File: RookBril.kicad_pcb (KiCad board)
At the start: 2 copper layers, 63 parts, among them J1 BATT_PINS, J10 UNCONNECTED_PB_PINS, J11 UNCONNECTED_PC_PINS, J12 PROGRAM_PINS, J13 3V_MODE_PINS, J2 IR_SENSOR0_PINS, J3 IR_SENSOR1_PINS, J4 IR_SENSOR2_PINS, J5 IR_SENSOR3_PINS, J6 LOW-BAT_LED_CONN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

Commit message: beginsel aan pcb gemaakt
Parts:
- added C24: 100n, Capacitor_SMD:C_0805_2012Metric_Pad1.18x1.45mm_HandSolder, F.Cu at (111.9, 149.8)
- J12: value PROGRAM_PINS -> Conn_01x04_Pin; footprint Connector_PinHeader_2.54mm:PinHeader_2x05_P2.54mm_Vertical -> Connector_PinHeader_2.54mm:PinHeader_1x04_P2.54mm_Vertical
- moved J1 120.0 mm to (30.7, 156.8), turned to 180 degrees
- moved J4 116.5 mm to (187.8, 156.0)
- moved R5 114.5 mm to (184.0, 155.8)
- moved R4 113.6 mm to (37.2, 160.5), turned to -90 degrees
- moved R3 112.0 mm to (37.0, 155.3), turned to -90 degrees
- moved C3 109.0 mm to (40.7, 160.5), turned to -90 degrees
- moved R1 108.3 mm to (184.0, 135.2)
- moved J12 107.3 mm to (135.9, 155.6)
- moved J2 107.0 mm to (187.8, 135.2)
- moved C13 105.5 mm to (106.7, 166.2), turned to 180 degrees
- moved J5 105.5 mm to (187.8, 145.7)
- moved R6 105.3 mm to (184.0, 145.5)
- moved C4 104.0 mm to (179.8, 156.8), turned to -90 degrees
- moved R2 99.8 mm to (184.0, 125.2)
- moved C15 97.0 mm to (99.9, 165.5), turned to 180 degrees
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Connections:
- J12 pad 1: +3V0 -> /MCU/SWDIO
- J12 pad 2: GND -> /MCU/SDCLK
- J12 pad 3: GND -> /MCU/NRST
- J12 pad 4: unconnected-(J12-Pin_4-Pad4) -> GND
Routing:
- net +3V0: track 0.00 -> 106.8 mm, vias 0 -> 6
- net /MCU/NRST: track 0.00 -> 55.0 mm
- net /MCU/SDCLK: track 0.00 -> 38.2 mm
- net +BATT: track 0.00 -> 29.8 mm
- net /MCU/SWDIO: track 0.00 -> 28.0 mm
- net VCC: track 0.00 -> 27.3 mm
- net VDDA: track 0.00 -> 18.5 mm
- net GND: track 0.00 -> 16.2 mm, vias 0 -> 2
- net Net-(D1-A): track 0.00 -> 15.1 mm
- net /PDLC-BOOST_VOUT-FB: track 0.00 -> 11.3 mm
- net /PDLC-BOOST_CTRL: track 0.00 -> 9.11 mm
- net /VBAT_FB: track 0.00 -> 6.87 mm
- net Net-(U2-FB): track 0.00 -> 5.89 mm
- net Net-(U4-FB): track 0.00 -> 5.52 mm
- net Net-(U4-MODE): track 0.00 -> 5.35 mm
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- added copper zone on B.Cu, net GND
- added copper zone on F.Cu, net GND

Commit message: Alle verbindingen gelegt van de componenten.
Moet nog bij nog tekst bij de connectoren zetten. Ook zijn de unconnected pinnen weggehaald, omdat het onmogelijk maakt voor een 2 laags PCB.
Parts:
- removed C19: 4.7u, Capacitor_SMD:C_0805_2012Metric_Pad1.18x1.45mm_HandSolder
- removed J11: UNCONNECTED_PC_PINS, Connector_PinHeader_1.00mm:PinHeader_1x14_P1.00mm_Vertical
- removed J8: UNCONNECTED_PA_PINS, Connector_PinHeader_1.00mm:PinHeader_1x07_P1.00mm_Vertical
- J10: value UNCONNECTED_PB_PINS -> TIM3_OUT_CONN; footprint Connector_PinHeader_1.00mm:PinHeader_1x13_P1.00mm_Vertical -> Connector_PinHeader_2.54mm:PinHeader_1x04_P2.54mm_Vertical
- moved C10 132.3 mm to (169.5, 86.3), turned to 180 degrees
- moved R11 130.4 mm to (169.5, 88.6), turned to 0 degrees
- moved R9 130.1 mm to (165.9, 87.2)
- moved C7 130.0 mm to (163.5, 82.9), turned to -90 degrees
- moved R12 129.2 mm to (162.5, 86.0)
- moved U2 128.5 mm to (166.1, 83.1)
- moved L1 127.5 mm to (166.7, 77.5)
- moved D1 126.9 mm to (171.4, 80.5)
- moved C8 126.5 mm to (169.5, 84.1)
- moved C6 112.4 mm to (162.5, 90.6), turned to 180 degrees
- moved R10 112.0 mm to (158.8, 89.6)
- moved R8 111.5 mm to (162.5, 88.3), turned to 0 degrees
- moved C9 110.7 mm to (158.4, 86.0), turned to 0 degrees
- moved R14 110.1 mm to (130.3, 91.3), turned to 90 degrees
- moved J7 109.0 mm to (176.7, 99.3)
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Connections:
- J10 pad 1: /MCU/PB2 -> /MCU/PB0
- J10 pad 2: /MCU/PB3 -> /MCU/PB1
- U3 pad 26: /IR_SIG2 -> /MCU/PB0
- U3 pad 27: /IR_SIG3 -> /MCU/PB1
- U3 pad 28: /MCU/PB2 -> /IR_SIG2
- U3 pad 30: Net-(U3-VCAP1) -> unconnected-(U3-VCAP1-Pad30)
- U3 pad 55: /MCU/PB3 -> /IR_SIG3
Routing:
- net +3V0: track 106.8 -> 170.6 mm, vias 6 -> 7
- net +BATT: track 29.8 -> 88.5 mm, vias 0 -> 1
- net /PDLC-BOOST_CTRL: track 9.11 -> 53.2 mm, vias 0 -> 2
- net /MCU/PB1: track 0.00 -> 38.5 mm, vias 0 -> 1
- net /MCU/PB0: track 0.00 -> 35.3 mm, vias 0 -> 1
- net /MCU/PB4: track 0.00 -> 35.0 mm, vias 0 -> 1
- net /MCU/PB5: track 0.00 -> 34.2 mm, vias 0 -> 1
- net /IR_SIG2: track 0.00 -> 32.7 mm, vias 0 -> 2
- net GND: track 16.2 -> 48.4 mm, vias 2 -> 32
- net /H-BRIDGE_IN_A: track 0.00 -> 32.1 mm, vias 0 -> 4
- net /IR_SIG3: track 0.00 -> 30.4 mm
- net /IR_SIG1: track 0.00 -> 28.3 mm
- net /VBAT_FB: track 6.87 -> 34.7 mm, vias 0 -> 2
- net /H-BRIDGE_SEL: track 0.00 -> 25.2 mm, vias 0 -> 2
- net Net-(J9-Pin_2): track 0.00 -> 24.9 mm
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- added copper zone on F.Cu, net +BATT
- added copper zone on F.Cu, net /PDLC-BOOST_VOUT-FB
- added copper zone on F.Cu, net VCC
- added copper zone on F.Cu, net VDDA
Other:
- board outline added: 65 x 55 mm

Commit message: nieuwe layout
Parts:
- moved J3 52.0 mm to (119.8, 95.9), turned to 180 degrees
- moved J6 47.8 mm to (118.5, 117.8)
- moved J9 47.5 mm to (105.6, 63.3)
- moved J12 46.9 mm to (129.6, 115.4), turned to 90 degrees
- moved R2 46.2 mm to (124.1, 96.0), turned to 180 degrees
- moved C2 45.0 mm to (124.0, 93.7)
- moved R17 43.8 mm to (134.7, 47.5)
- moved R14 43.8 mm to (132.5, 47.6)
- moved R16 43.8 mm to (137.8, 46.7)
- moved C22 43.8 mm to (136.0, 43.1)
- moved C23 43.8 mm to (130.6, 43.2)
- moved R15 43.8 mm to (129.2, 46.8)
- moved L2 43.8 mm to (133.2, 40.6)
- moved U4 43.8 mm to (133.3, 43.3)
- moved J2 39.1 mm to (119.8, 104.9), turned to 180 degrees
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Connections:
- U3 pad 15: /H-BRIDGE_IN_A -> /H-BRIDGE_IN_B
- U3 pad 16: /H-BRIDGE_IN_B -> /H-BRIDGE_IN_A
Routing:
- net +3V0: track 170.6 -> 27.6 mm, vias 7 -> 0
- net +BATT: track 88.5 -> 0.00 mm, vias 1 -> 0
- net /MCU/PB1: track 38.5 -> 0.00 mm, vias 1 -> 0
- net /MCU/PB0: track 35.3 -> 0.00 mm, vias 1 -> 0
- net /MCU/PB4: track 35.0 -> 0.00 mm, vias 1 -> 0
- net /VBAT_FB: track 34.7 -> 0.00 mm, vias 2 -> 0
- net /MCU/PB5: track 34.2 -> 0.00 mm, vias 1 -> 0
- net /IR_SIG2: track 32.7 -> 0.00 mm, vias 2 -> 0
- net /PDLC-BOOST_CTRL: track 53.2 -> 20.8 mm
- net /IR_SIG1: track 28.3 -> 0.00 mm
- net Net-(J9-Pin_2): track 24.9 -> 0.00 mm
- net /MCU/NRST: track 45.6 -> 21.6 mm, vias 2 -> 0
- net /IR_SIG3: track 30.4 -> 10.5 mm
- net /MCU/SDCLK: track 30.4 -> 13.6 mm, vias 2 -> 0
- net /IR_SIG0: track 16.7 -> 0.00 mm
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- removed copper zone on F.Cu, net /PDLC-BOOST_VOUT-FB
- removed copper zone on F.Cu, net VDDA
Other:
- board text added: "NRST"
- board text added: "RESET"
- board text added: "SDCLK"
- board text added: "SWD"
- board text added: "SWDIO"

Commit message: betere
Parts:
- moved J9 72.0 mm to (148.4, 121.2), turned to -90 degrees
- moved J10 64.2 mm to (168.7, 96.9), turned to 0 degrees
- moved R3 44.2 mm to (132.2, 89.2)
- moved R4 44.2 mm to (132.2, 93.4)
- moved C3 44.2 mm to (136.0, 93.4)
- moved J13 39.6 mm to (130.5, 71.3), turned to 90 degrees
- moved R15 38.2 mm to (134.1, 84.6)
- moved J1 36.6 mm to (124.7, 81.4)
- moved C22 36.5 mm to (135.4, 79.6)
- moved C23 36.5 mm to (130.0, 79.7)
- moved R16 36.5 mm to (137.2, 83.2)
- moved L2 36.5 mm to (132.6, 77.1)
- moved R17 36.5 mm to (134.1, 84.0)
- moved U4 36.5 mm to (132.6, 79.8)
- moved R14 36.5 mm to (131.9, 84.1)
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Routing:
- net GND: track 34.7 -> 26.4 mm, vias 23 -> 24
- net VCC: track 28.3 -> 35.8 mm, vias 0 -> 2
- net /VBAT_FB: track 0.00 -> 5.97 mm
- net /H-BRIDGE_SEL: track 27.7 -> 22.6 mm
- net VDDA: track 2.81 -> 7.15 mm
- net /H-BRIDGE_PWM: track 25.4 -> 21.2 mm
- net /H-BRIDGE_IN_B: track 22.7 -> 18.8 mm
- net /H-BRIDGE_IN_A: track 18.2 -> 15.6 mm
- net Net-(J7-Pin_2): track 14.9 -> 12.6 mm
- net /IR_SIG3: track 10.5 -> 12.2 mm
- net Net-(J5-Pin_1): track 3.22 -> 4.14 mm
- net /MCU/NRST: track 21.6 -> 22.3 mm
- net +3V0: track 27.6 -> 27.0 mm

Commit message: bijna alle verbindingen gelegd
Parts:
- moved C6 18.1 mm to (164.8, 83.5), turned to 0 degrees
- moved J1 13.5 mm to (133.4, 71.0), turned to -90 degrees
- moved J13 9.49 mm to (124.7, 78.8), turned to 0 degrees
- moved R4 7.10 mm to (134.8, 86.8), turned to 180 degrees
- moved R16 7.02 mm to (131.0, 86.5), turned to 90 degrees
- moved R15 7.02 mm to (130.3, 78.7)
- moved R3 6.86 mm to (138.7, 86.8), turned to 180 degrees
- moved L2 6.39 mm to (137.3, 81.4), turned to -90 degrees
- moved C23 4.75 mm to (134.6, 78.7), turned to 180 degrees
- moved C3 4.63 mm to (134.8, 89.0), turned to 180 degrees
- moved C22 4.60 mm to (134.7, 84.2), turned to 180 degrees
- moved R17 3.88 mm to (130.3, 83.4), turned to 180 degrees
- moved R14 3.23 mm to (130.3, 81.3), turned to 0 degrees
- moved J10 2.62 mm to (171.1, 97.8)
- moved U4 2.48 mm to (134.5, 81.4), turned to 180 degrees
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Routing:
- net /MCU/PB1: track 0.00 -> 32.7 mm, vias 0 -> 1
- net /MCU/PB0: track 0.00 -> 31.2 mm, vias 0 -> 1
- net /IR_SIG0: track 0.00 -> 31.1 mm
- net /MCU/PB4: track 0.00 -> 29.7 mm, vias 0 -> 1
- net /MCU/PB5: track 0.00 -> 28.8 mm, vias 0 -> 1
- net /IR_SIG1: track 0.00 -> 25.3 mm
- net /IR_SIG2: track 0.00 -> 22.1 mm
- net /MCU/NRST: track 22.3 -> 43.3 mm, vias 0 -> 2
- net Net-(J9-Pin_2): track 0.00 -> 17.2 mm
- net GND: track 26.4 -> 39.8 mm, vias 24 -> 37
- net /VBAT_FB: track 5.97 -> 16.9 mm, vias 0 -> 2
- net +BATT: track 0.00 -> 9.78 mm
- net Net-(J6-Pin_2): track 0.00 -> 3.08 mm
- net /MCU/LOW-BAT_LED_EN: track 0.00 -> 2.36 mm
- net +3V0: track 27.0 -> 29.2 mm
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- removed copper zone on F.Cu, net VCC

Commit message: Alles klaar 1 error, en nog silkscreen fixen
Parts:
- moved J10 1.73 mm to (171.2, 96.1)
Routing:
- net +3V0: track 29.2 -> 82.8 mm, vias 0 -> 16
- net Net-(J13-Pin_2): track 0.00 -> 4.60 mm
- net /MCU/PB4: track 29.7 -> 32.9 mm
- net /MCU/PB5: track 28.8 -> 31.9 mm
- net /PDLC-BOOST_CTRL: track 20.8 -> 22.0 mm
- net /IR_SIG2: track 22.1 -> 21.4 mm
- net GND: track 39.8 -> 40.3 mm, vias 37 -> 61
- added copper zone on B.Cu, net +3V0

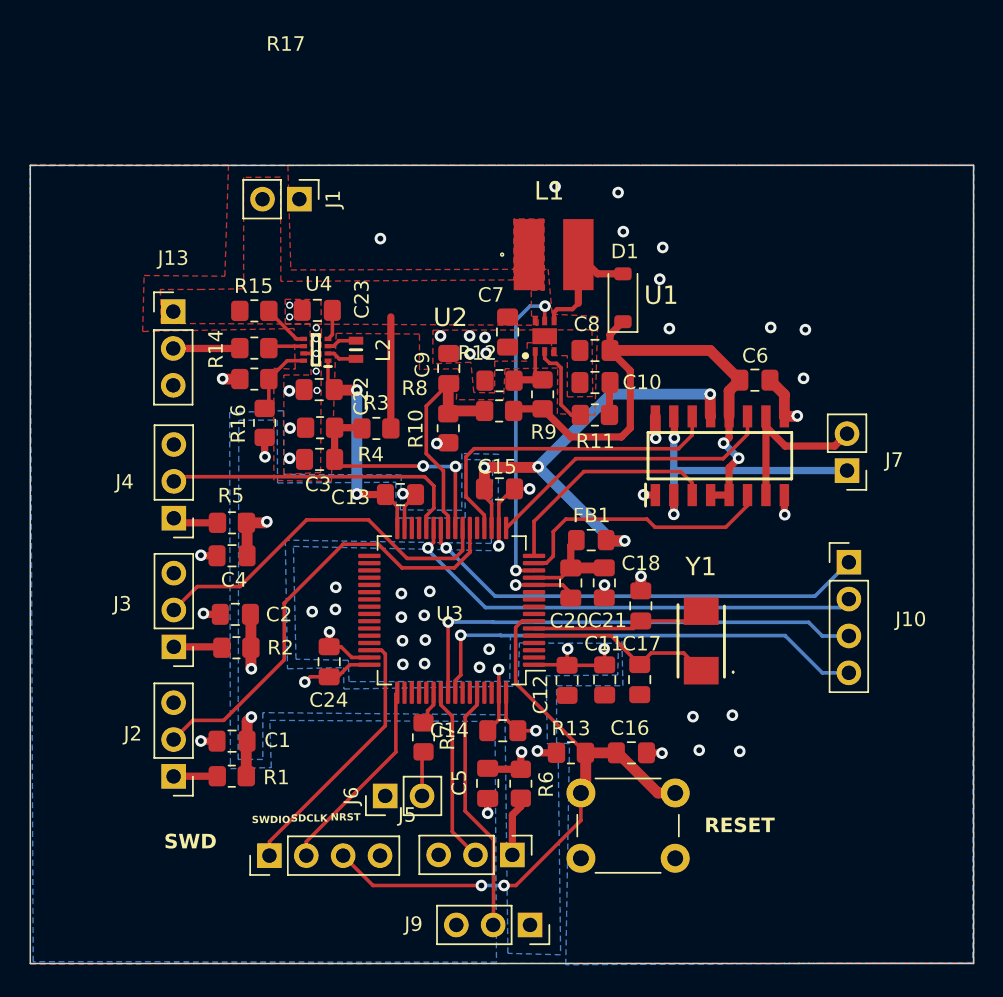
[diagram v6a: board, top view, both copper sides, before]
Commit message: Klein beetje reorganiseren van de lay-out Silkscreen schoongemaakt TestPoints en Mounting holes toegevoegd
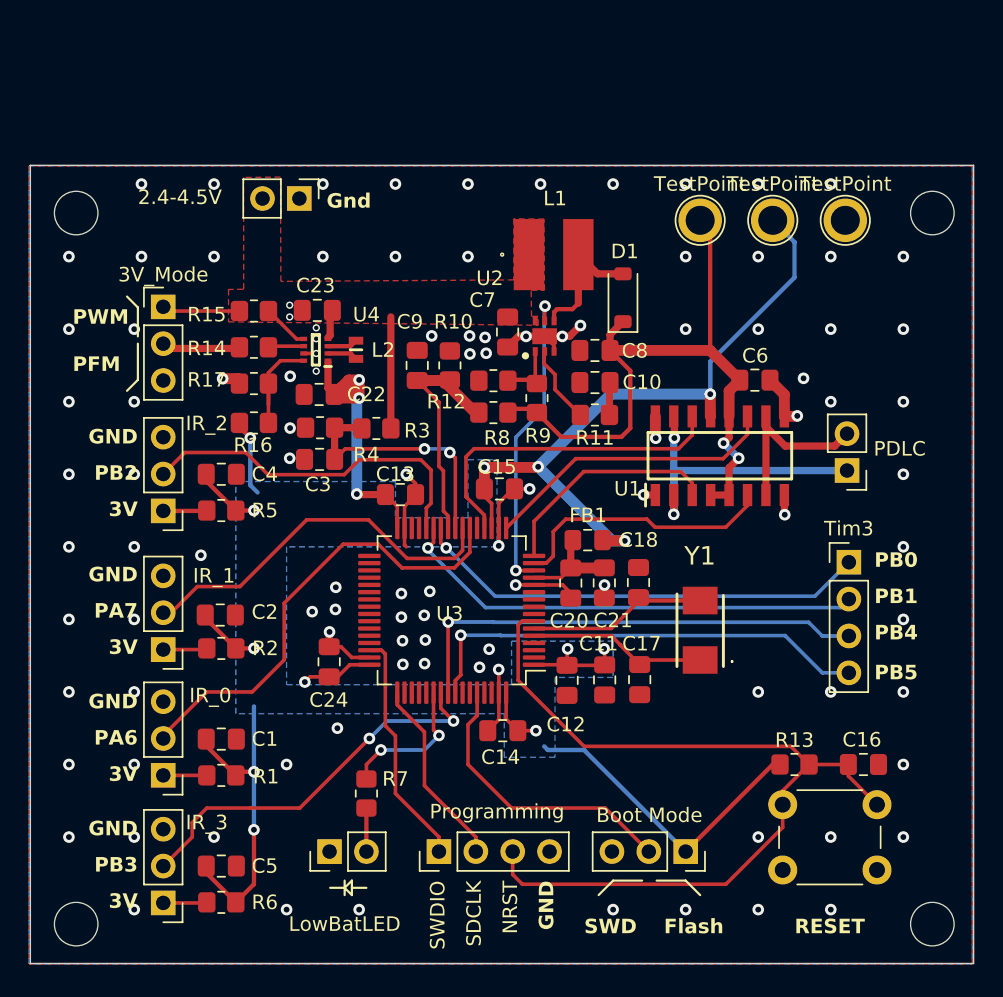
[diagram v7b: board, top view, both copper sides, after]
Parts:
- added H1: MountingHole, MountingHole:MountingHole_3mm, F.Cu at (177.0, 72.0)
- added H2: MountingHole, MountingHole:MountingHole_3mm, F.Cu at (177.0, 121.0)
- added H3: MountingHole, MountingHole:MountingHole_3mm, F.Cu at (118.0, 72.0)
- added H4: MountingHole, MountingHole:MountingHole_3mm, F.Cu at (118.0, 121.0)
- added TP1: TestPoint, TestPoint:TestPoint_Plated_Hole_D2.0mm, F.Cu at (166.0, 72.5)
- added TP2: TestPoint, TestPoint:TestPoint_Plated_Hole_D2.0mm, F.Cu at (161.0, 72.5)
- added TP4: TestPoint, TestPoint:TestPoint_Plated_Hole_D2.0mm, F.Cu at (171.0, 72.5)
- moved J5 24.3 mm to (124.0, 119.5), turned to 180 degrees
- moved R6 22.2 mm to (128.0, 119.5), turned to 180 degrees
- moved C5 19.2 mm to (128.0, 117.0), turned to 0 degrees
- moved C16 16.0 mm to (172.2, 110.0)
- moved R13 15.4 mm to (167.5, 110.0)
- moved SW1 13.9 mm to (166.7, 112.8)
- moved J9 11.9 mm to (160.0, 116.0)
- moved J12 11.7 mm to (143.0, 116.0)
- moved C4 5.66 mm to (128.0, 90.0), turned to 0 degrees
- moved R7 5.52 mm to (138.0, 112.0)
- moved J6 5.42 mm to (135.5, 116.0)
- moved R10 4.33 mm to (143.8, 82.5), turned to -90 degrees
- moved C9 2.18 mm to (141.5, 82.5)
- moved C18 1.62 mm to (156.8, 97.5)
- moved R5 1.12 mm to (128.0, 92.5)
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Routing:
- net +3V0: track 82.8 -> 146.3 mm
- net /MCU/NRST: track 43.3 -> 60.9 mm, vias 2 -> 0
- net /IR_SIG3: track 12.2 -> 27.0 mm, vias 0 -> 2
- net VCC: track 37.4 -> 46.6 mm
- net /MCU/LOW-BAT_LED_EN: track 2.36 -> 9.93 mm, vias 0 -> 2
- net +BATT: track 9.78 -> 14.3 mm
- net /IR_SIG2: track 21.4 -> 24.6 mm
- net Net-(J9-Pin_2): track 17.2 -> 20.2 mm
- net Net-(U4-FB): track 5.07 -> 7.68 mm
- net /PDLC-BOOST_VOUT-FB: track 15.9 -> 18.5 mm
- net /MCU/SWDIO: track 18.4 -> 16.4 mm
- net GND: track 40.3 -> 42.1 mm, vias 61 -> 106
- net Net-(J5-Pin_1): track 4.14 -> 3.02 mm
- net /VBAT_FB: track 16.9 -> 17.8 mm
- net /IR_SIG0: track 31.1 -> 31.9 mm
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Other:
- board text added: "2.4-4.5V"
- board text added: "3V"
- board text added: "Flash"
- board text added: "GND"
- board text added: "Gnd"
- board text added: "PA6"
- board text added: "PA7"
- board text added: "PB0"
- board text added: "PB1"
- board text added: "PB2"
- board text added: "PB3"
- board text added: "PB4"
- board text added: "PB5"
- board text added: "PFM"
- board text added: "PWM"

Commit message: Kleine veranderingen gebaseerd op feedback whatsapp
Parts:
- added TP3: TestPoint, Components:exposedPad5x10, F.Cu at (177.2, 79.5)
- C11: value 4.7u -> 10u
- C22: value 47u -> 10u
- C23: value 22u -> 10u
- J9: footprint Connector_PinSocket_2.54mm:PinSocket_1x03_P2.54mm_Vertical -> Connector_PinHeader_2.54mm:PinHeader_1x03_P2.54mm_Vertical
- moved C16 1.25 mm to (171.0, 110.0)
- moved R13 1.00 mm to (166.5, 110.0)
- moved SW1 0.69 mm to (166.0, 112.8)
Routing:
- net /MCU/NRST: track 60.9 -> 59.5 mm
- net +3V0: track 146.3 -> 145.6 mm
